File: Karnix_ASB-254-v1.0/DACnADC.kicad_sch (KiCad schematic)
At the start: 84 parts, among them U11 LM258A, U14 LM258A, U4 AD5328BRUZ, U7 ADC128S052CIMT

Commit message: Remove rudimentary referencies to old projects
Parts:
- gave numbers to parts that had none: 2
- renumbered C35 to C65, C27 to C66, C25 to C67, C27 to C68, C29 to C69, C40 to C70, C40 to C71, C41 to C72, C41 to C73, C44 to C74, C44 to C75, C48 to C76, C48 to C77, C52 to C78, C52 to C79, C56 to C80, C56 to C81, C40 to C84, C48 to C86, D10 to D12, D10 to D13, D15 to D14, D10 to D16, D10 to D17, D19 to D18, D15 to D20, L5 to L10, L5 to L11, L5 to L12, L5 to L13, L5 to L14, L5 to L15, L5 to L16, L4 to L5, L4 to L6, L5 to L7, L5 to L8, L5 to L9, R26 to R123, R26 to R124, R30 to R125, R30 to R126, R122 to R127, R122 to R128, R34 to R129, R34 to R130, R38 to R131, R38 to R132, R42 to R133, R42 to R134, R46 to R135, R46 to R136, R122 to R137, R122 to R138, R50 to R139, R50 to R140, R54 to R141, R54 to R142, R204 to R143, R204 to R144, R208 to R145, R208 to R146, R26 to R147, R30 to R148, R42 to R149, R38 to R150, R42 to R151, R208 to R156, R42 to R157, U7 to U10, U4 to U11, U14 to U12, U11 to U12, U11 to U13, U14 to U13, U11 to U14, U11 to U15, U11 to U16, U14 to U16

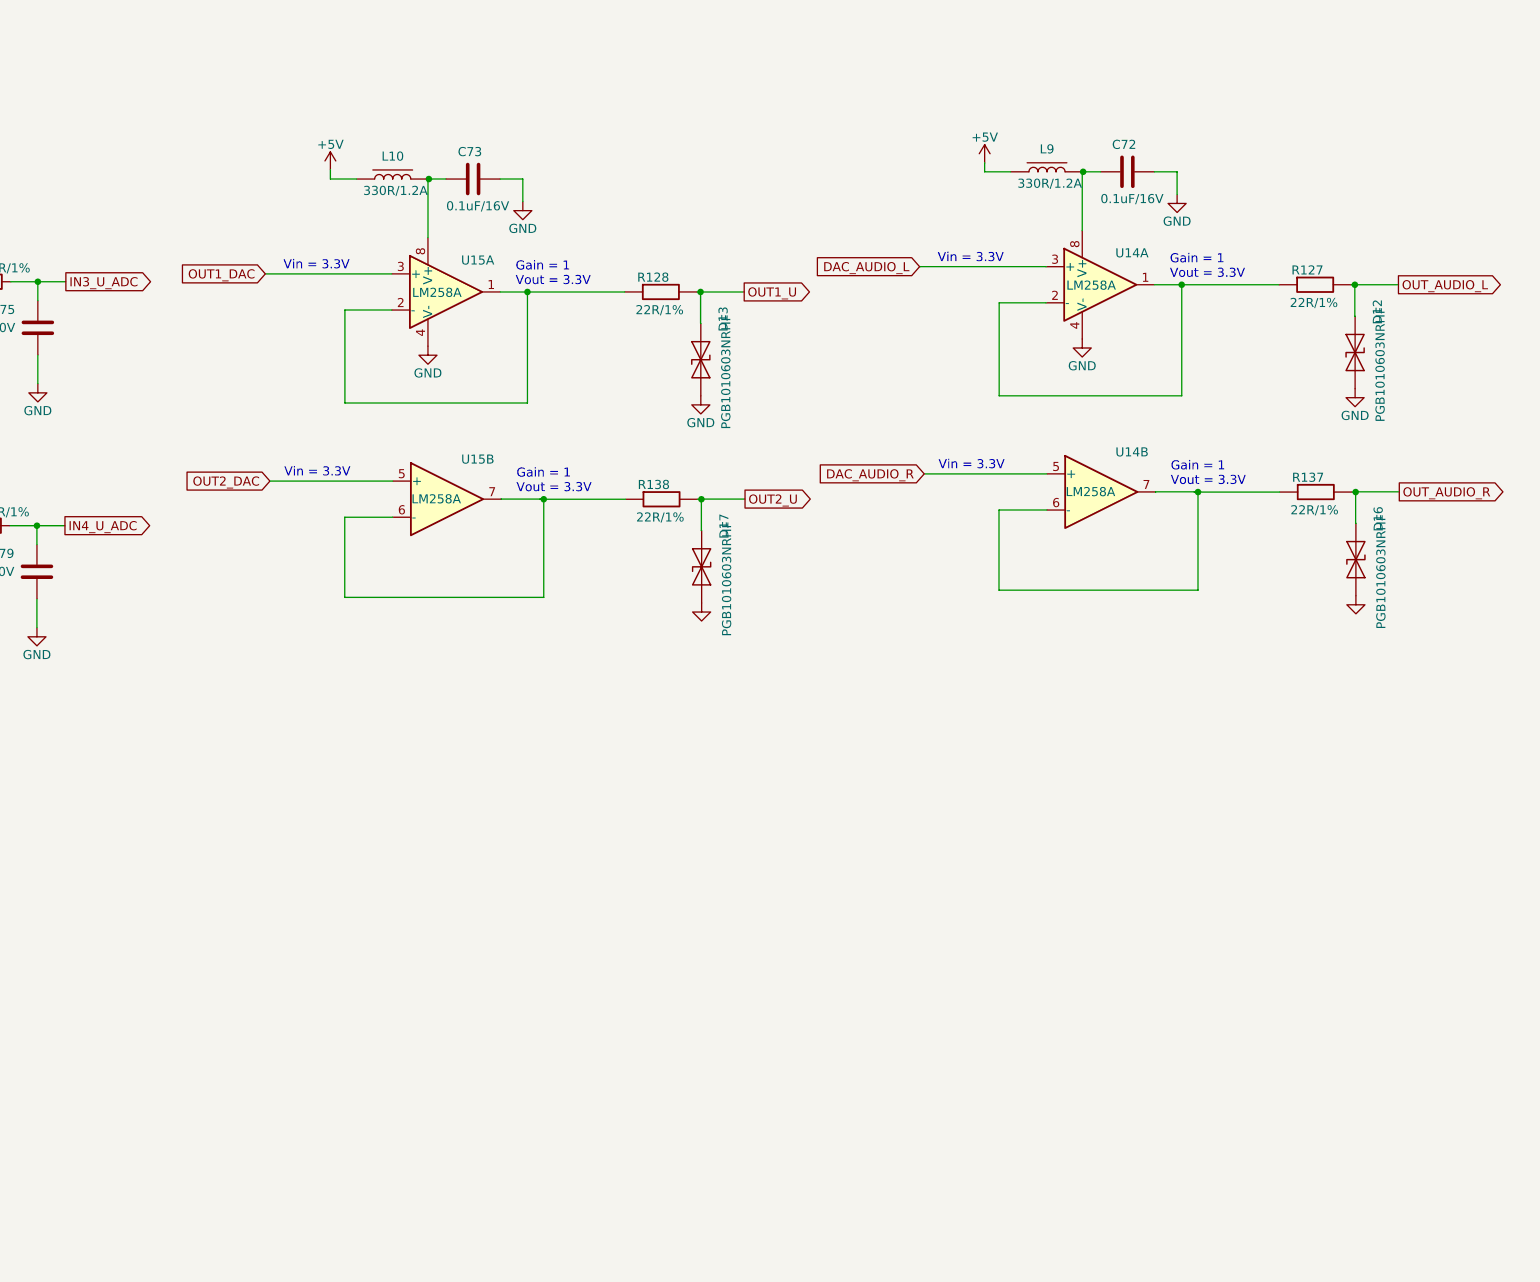
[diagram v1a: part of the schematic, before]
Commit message: Fix ESD protection for Audio L/R signals
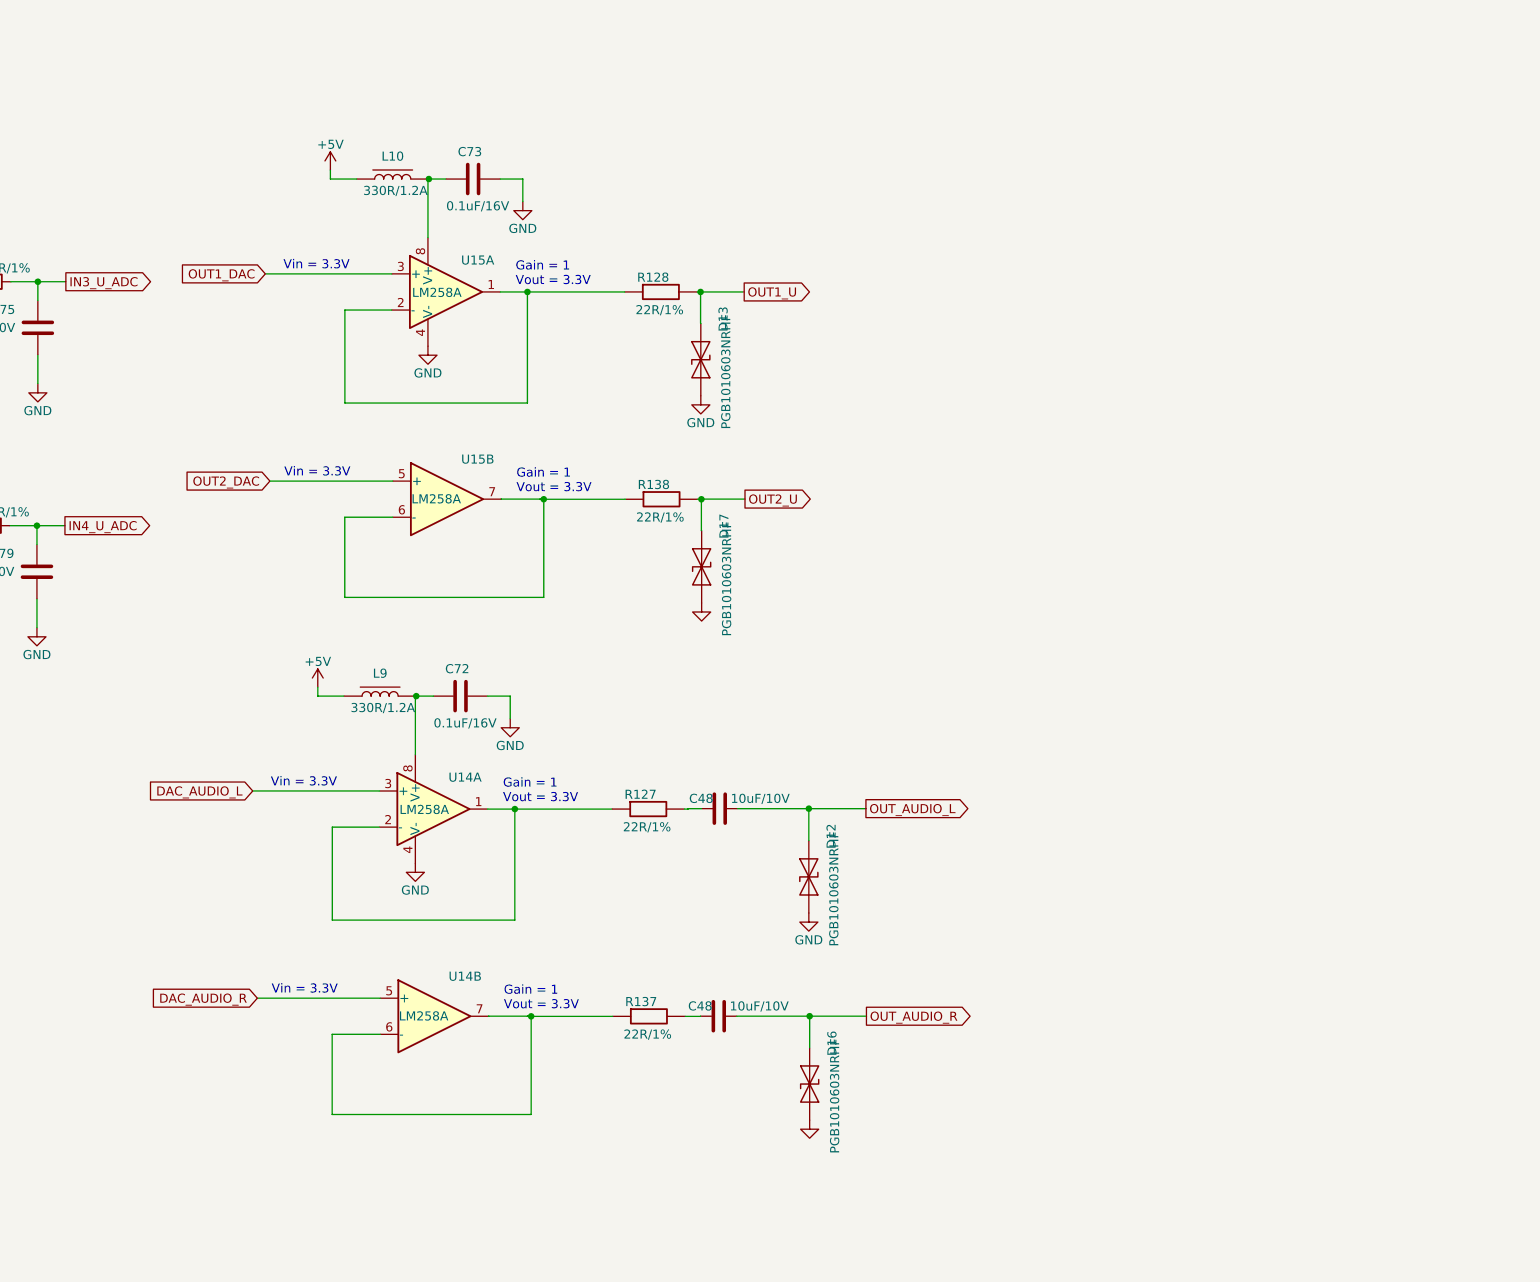
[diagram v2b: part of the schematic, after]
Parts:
- added C48 (x2): 10uF/10V, Capacitor_SMD:C_0603_1608Metric, symbol Fabmicro:CapacitorUnpolarized
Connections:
- net OUT_AUDIO_L: now also C48.2; no longer R127.1
- net OUT_AUDIO_R: now also C48.2; no longer R137.1
- new net: C48.1, R127.1
- new net: C48.1, R137.1
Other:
- moved on the sheet: C72, D12, D16, L9, R127, R137, U14A, U14B
